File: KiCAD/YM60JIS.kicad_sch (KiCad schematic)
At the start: 165 parts, among them J1 TYPE-C-31-M-12, SW1 SW_Push, SW10 SW_Push, SW11 SW_Push, SW12 SW_Push, SW13 SW_Push, SW14 SW_Push, SW15 SW_Push, SW16 SW_Push, SW17 SW_Push, SW18 SW_Push, SW19 SW_Push, SW2 SW_Push, SW20 SW_Push, SW21 SW_Push, SW22 SW_Push, SW23 SW_Push, SW24 SW_Push, SW25 SW_Push, SW26 SW_Push, SW27 SW_Push, SW28 SW_Push, SW29 Space, SW3 SW_Push, SW30 SW_Push, SW31 SW_Push, SW32 SW_Push, SW33 SW_Push, SW34 SW_Push, SW35 SW_Push, SW36 SW_Push, SW37 SW_Push, SW38 SW_Push, SW39 SW_Push, SW4 SW_Push, SW40 SW_Push, SW41 SW_Push, SW42 SW_Push, SW43 SW_Push, SW44 SW_Push, SW45 SW_Push, SW46 SW_Push, SW47 SW_Push, SW48 SW_Push, SW49 SW_Push, SW5 SW_Push, SW50 SW_Push, SW51 SW_Push, SW52 SW_Push, SW53 SW_Push, SW54 SW_Push, SW55 SW_Push, SW56 SW_Push, SW57 SW_Push, SW58 SW_Push, SW59 SW_Push, SW6 SW_Push, SW60 SW_Push, SW61 SW_Push, SW62 SW_Push, SW63 Yen, SW64 Backspace, SW65 ISOEnter, SW66 SW_Push, SW67 SW_Push, SW7 SW_Push, SW8 SW_Push, SW9 SW_Push, U1 XC6206P332MR, U2 SMF05CT1G, U3 RP2040, U4 W25Q16JVUXIQ, Y1 X322512MSB4SI

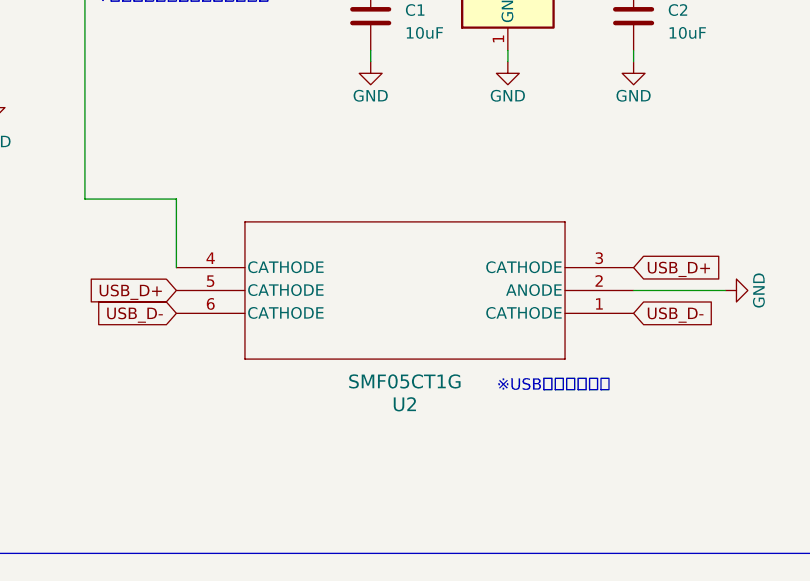
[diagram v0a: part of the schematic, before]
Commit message: JLCPCGのPCBAで向きが誤っている部品にJLCPCB Rotation Offset指示を追加
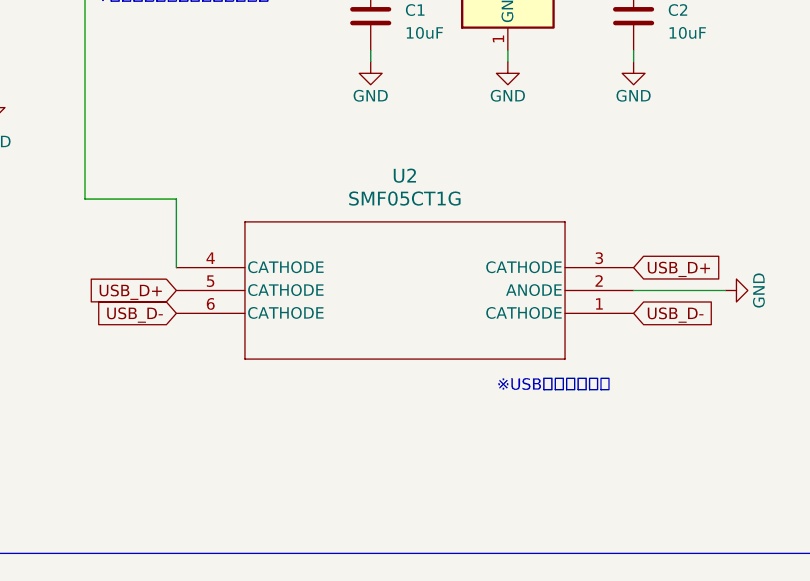
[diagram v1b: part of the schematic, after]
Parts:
- U2, U4: JLCPCB Rotation Offset (none) -> 180
